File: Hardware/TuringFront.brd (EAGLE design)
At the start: 107 x 49.5 mm, 73 parts, among them T1 2N3904, U1 TL074_

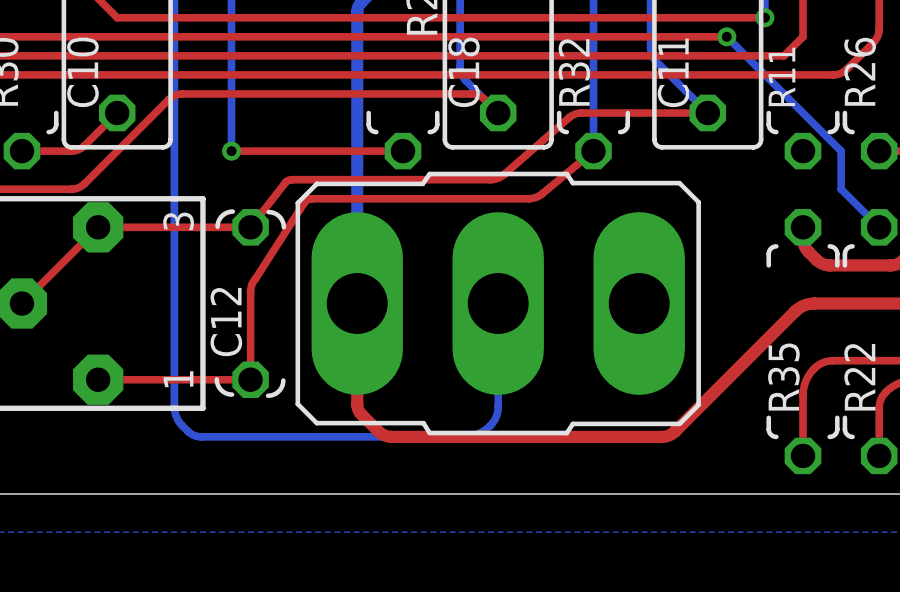
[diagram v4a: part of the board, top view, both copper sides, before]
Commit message: Front board updated with new Write switch component
Slightly enlarged holes to accommodate 2.03 x 0.76 solder tags
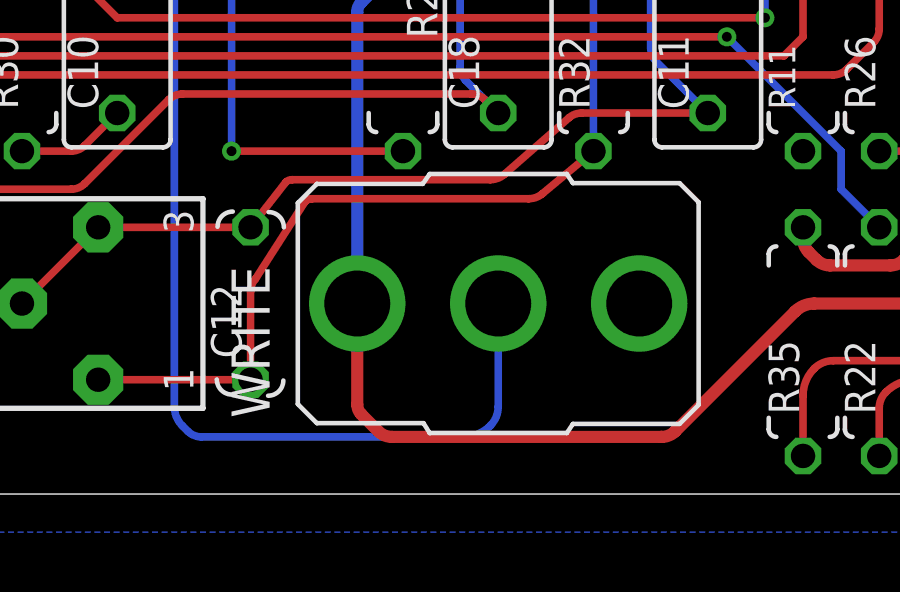
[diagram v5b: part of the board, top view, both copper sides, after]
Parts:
- WRITE: device TomW:M9040P -> MusicThingModular:M9040P
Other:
- board text added: "Music Thing Modular Turing Machine Rev 4 Front Board February 2016 CC-BY-SA"
- board text removed: "Music Thing Modular Turing Machine Rev 4 Front Board September 2015 CC-BY-SA"
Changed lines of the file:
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@@
 <text x="81.28" y="38.1" size="1.27" layer="22" font="vector" ratio="12" distance="40" rot="MR270" align="top-left">Music Thing Modular Turing Machine
 Rev 4 Front Board
-September 2015 CC-BY-SA
+February 2016 CC-BY-SA
 </text>
 <wire x1="85.725" y1="36.83" x2="84.455" y2="36.83" width="0.4064" layer="51"/>
@@
 <element name="R3" library="TomW" package="0207/7" value="68k" x="27.94" y="36.83" rot="R90"/>
 <element name="R9" library="TomW" package="0207/7" value="15k" x="30.48" y="36.83" rot="R90"/>
-<element name="WRITE" library="TomW" package="M9040P" value="T-80-T-SPDT-ON-OFF-ON" x="49.53" y="6.35" smashed="yes" rot="R90"/>
+<element name="WRITE" library="MusicThingModular" package="M9040P" value="T-80-T-SPDT-ON-OFF-ON" x="49.53" y="6.35" rot="R90"/>
 <element name="R18" library="TomW" package="0207/7" value="1k" x="35.56" y="36.83" rot="R90"/>
 <element name="R22" library="TomW" package="0207/7" value="100k" x="62.23" y="5.08" rot="R90"/>
